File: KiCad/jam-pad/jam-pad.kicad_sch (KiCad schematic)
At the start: 61 parts

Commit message: update gitignore, some unknown schematic changes
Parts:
- added J?: Conn_01x03, symbol Connector_Generic:Conn_01x03
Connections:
- net DIG0 is gone; now on net Row0: U?.2 (GPIO0)
- net DIG1 is gone; now on net Row1: U?.3 (GPIO1)
- net DIG10 is gone; now on net CS: U?.13 (GPIO10)
- net DIG11 is gone; now on net DC: U?.14 (GPIO11)
- net DIG12 is gone; now on net OLED_RST: U?.15 (GPIO12)
- net DIG13 is gone; now on net ENC_A: U?.16 (GPIO13)
- net DIG14 is gone; now on net ENC_C: U?.17 (GPIO14)
- net DIG15 is gone; now on net ENC_B: U?.18 (GPIO15)
- net DIG2 is gone; now on net Row2: U?.4 (GPIO2)
- net DIG3 is gone; now on net Col0: U?.5 (GPIO3)
- net DIG4 is gone; now on net Col1: U?.6 (GPIO4)
- net DIG5 is gone; now on net Col2: U?.7 (GPIO5)
- net DIG6 is gone; now on net Col3: U?.8 (GPIO6)
- net DIG7 is gone; now on net Col4: U?.9 (GPIO7)
- net DIG8 is gone; now on net MOSI: U?.11 (GPIO8)
- net DIG9 is gone; now on net SCLK: U?.12 (GPIO9)
- net GND: now also J?.2 (Pin_2)
- net SWCLK: now also J?.3 (Pin_3)
- net SWDIO: now also J?.1 (Pin_1)
- net at U?.21 (XOUT): now also C?.2, Y?.1
- net ~{DIR_OUT_A}: no longer names the net of U?.27 (GPIO16)
- net ~{DIR_OUT_B}: no longer names the net of U?.29 (GPIO18)
- net ~{OE_A}: no longer names the net of U?.28 (GPIO17)
- net ~{OE_B}: no longer names the net of U?.30 (GPIO19)
- no-connect marks 5 -> 9

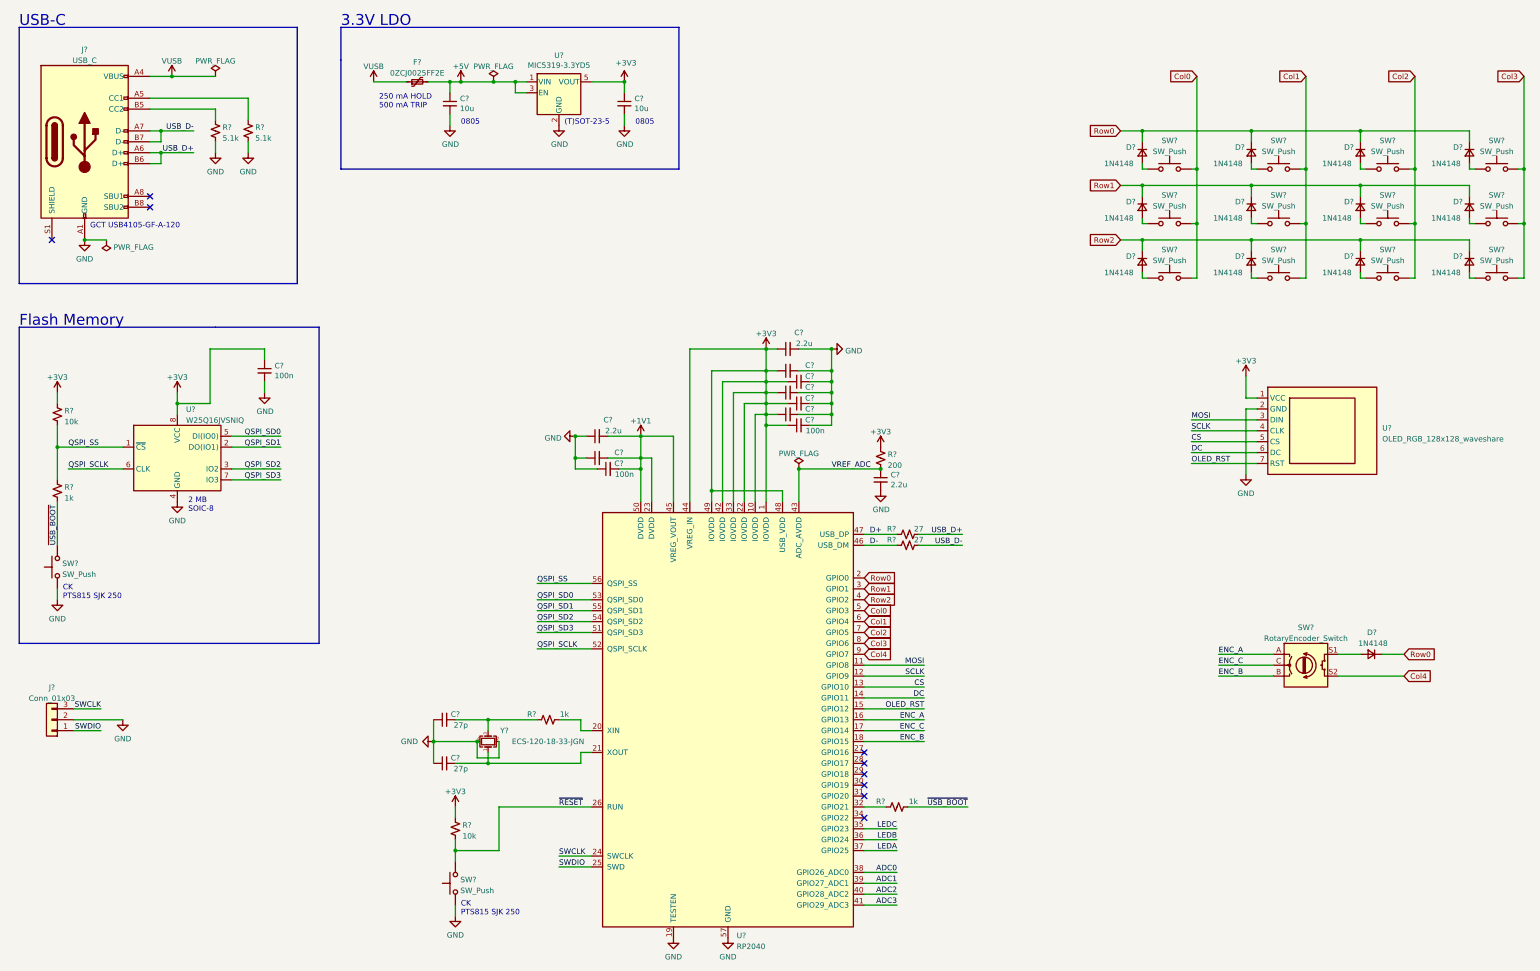
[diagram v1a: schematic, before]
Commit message: Assign footprints
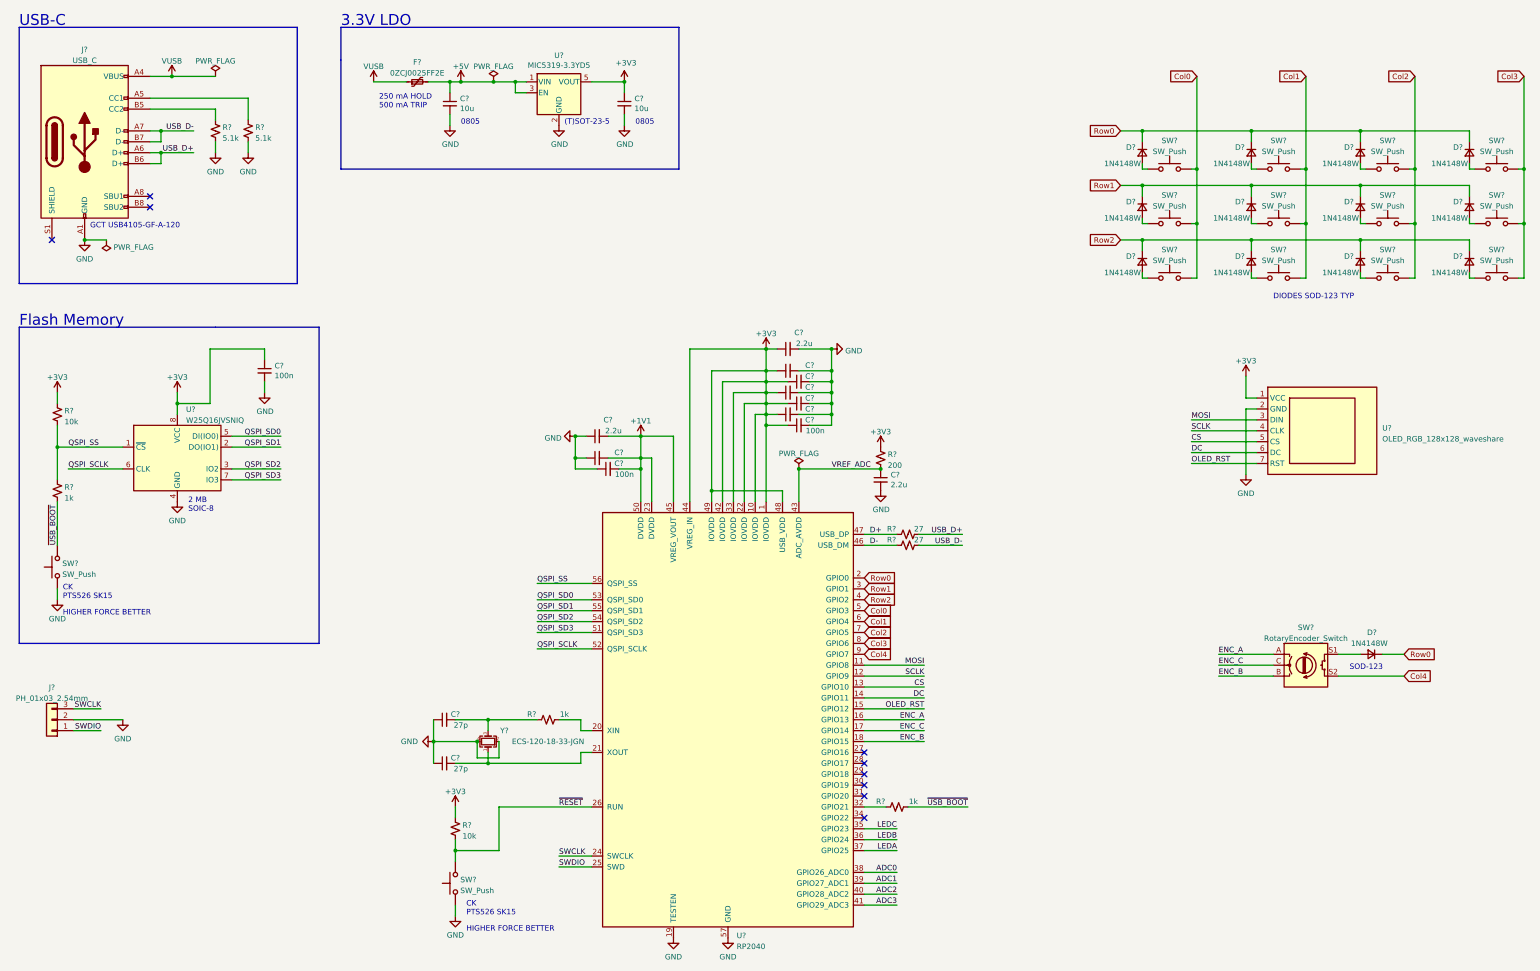
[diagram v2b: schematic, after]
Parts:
- D? (x13): value 1N4148 -> 1N4148W; footprint (none) -> Diode_SMD:D_SOD-123
- J?: value Conn_01x03 -> PH_01x03_2.54mm; footprint (none) -> jam-pad:PinHeader_1x03_P2.54mm_NoSilk
- SW? (x12): footprint (none) -> Keebio-Parts:Kailh-PG1350-1u-NoLED
- SW? (x2): footprint jackrabbit:SW_Push_CK_PTS815_HandSoldering -> jam-pad:SW_Push_PTS526
- SW?: footprint (none) -> Rotary_Encoder:RotaryEncoder_Alps_EC11E-Switch_Vertical_H20mm
- U?: footprint (none) -> jam-pad:Display_Waveshare_OLED_1.5inch_128x128
- U?: footprint jackrabbit:RP2040-QFN-56_HandSoldering -> jam-pad:RP2040-QFN-56_HandSoldering
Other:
- note added: "CK PTS526 SK15"
- note added: "DIODES SOD-123 TYP"
- note added: "HIGHER FORCE BETTER"
- note added: "SOD-123"
- note removed: "CK PTS815 SJK 250"
- title: (none) -> JamPad

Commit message: mx_only fp lib and replace switch footprints
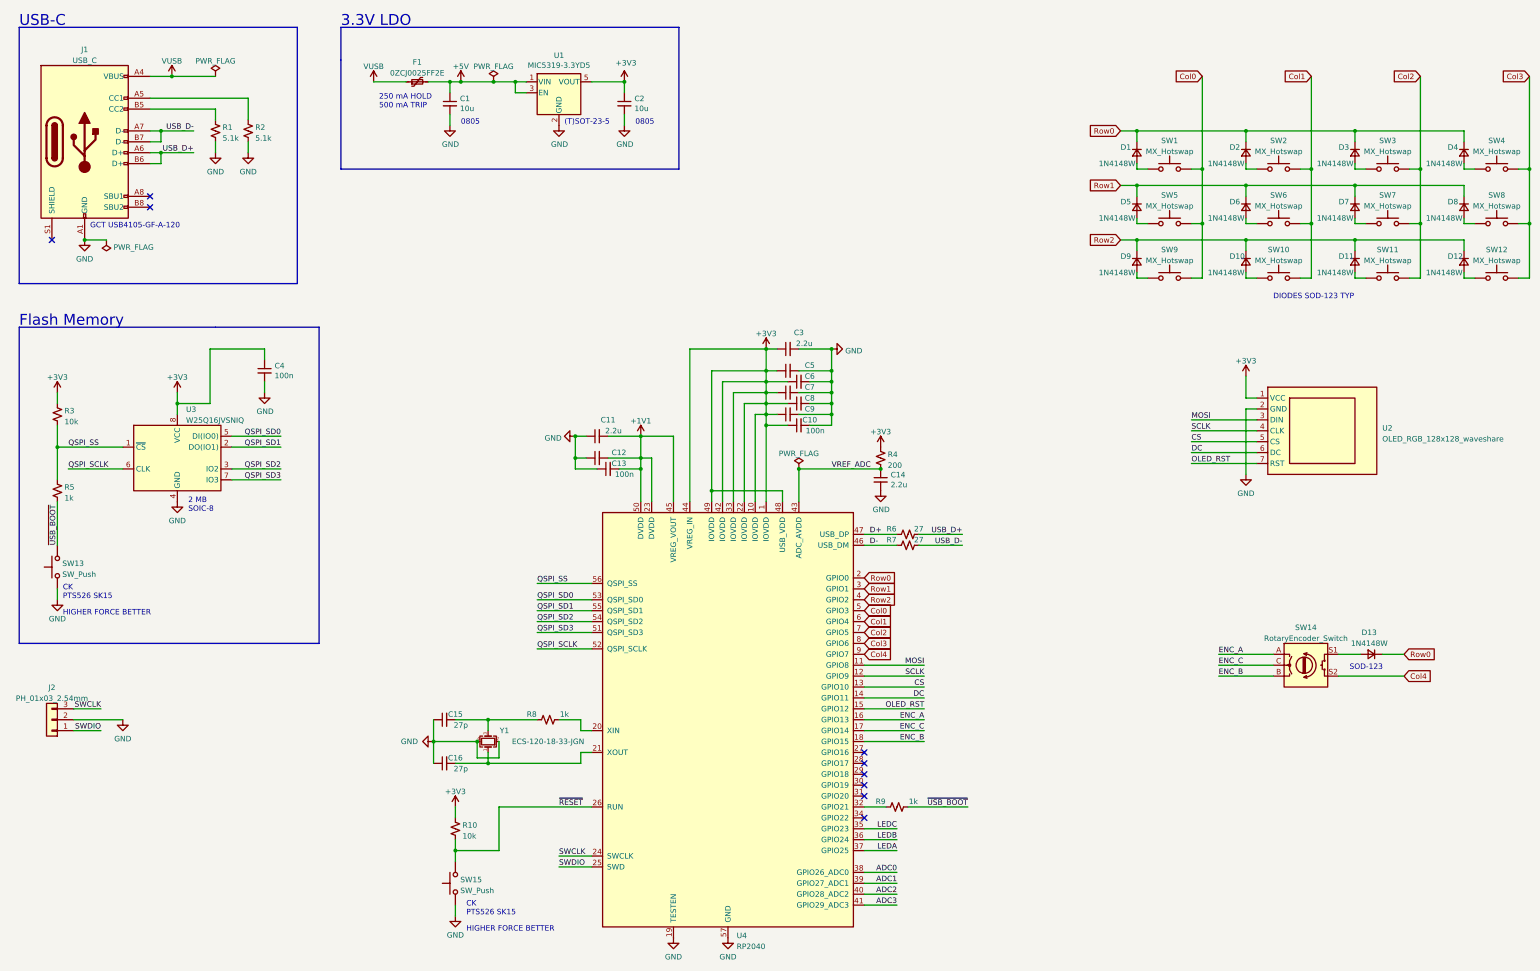
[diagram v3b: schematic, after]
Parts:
- SW1, SW10, SW11, SW12, SW2, SW3, SW4, SW5, SW6, SW7, SW8, SW9: renamed from SW?; value SW_Push -> MX_Hotswap; footprint Keebio-Parts:Kailh-PG1350-1u-NoLED -> MX_Only:MXOnly-1U-Hotswap-LED
- gave numbers to parts that had none: 50
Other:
- moved on the sheet: D1, D10, D11, D12, D2, D3, D4, D5, D6, D7, D8, D9

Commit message: Clean up symbol dependencies and pass ERC with schematic so far
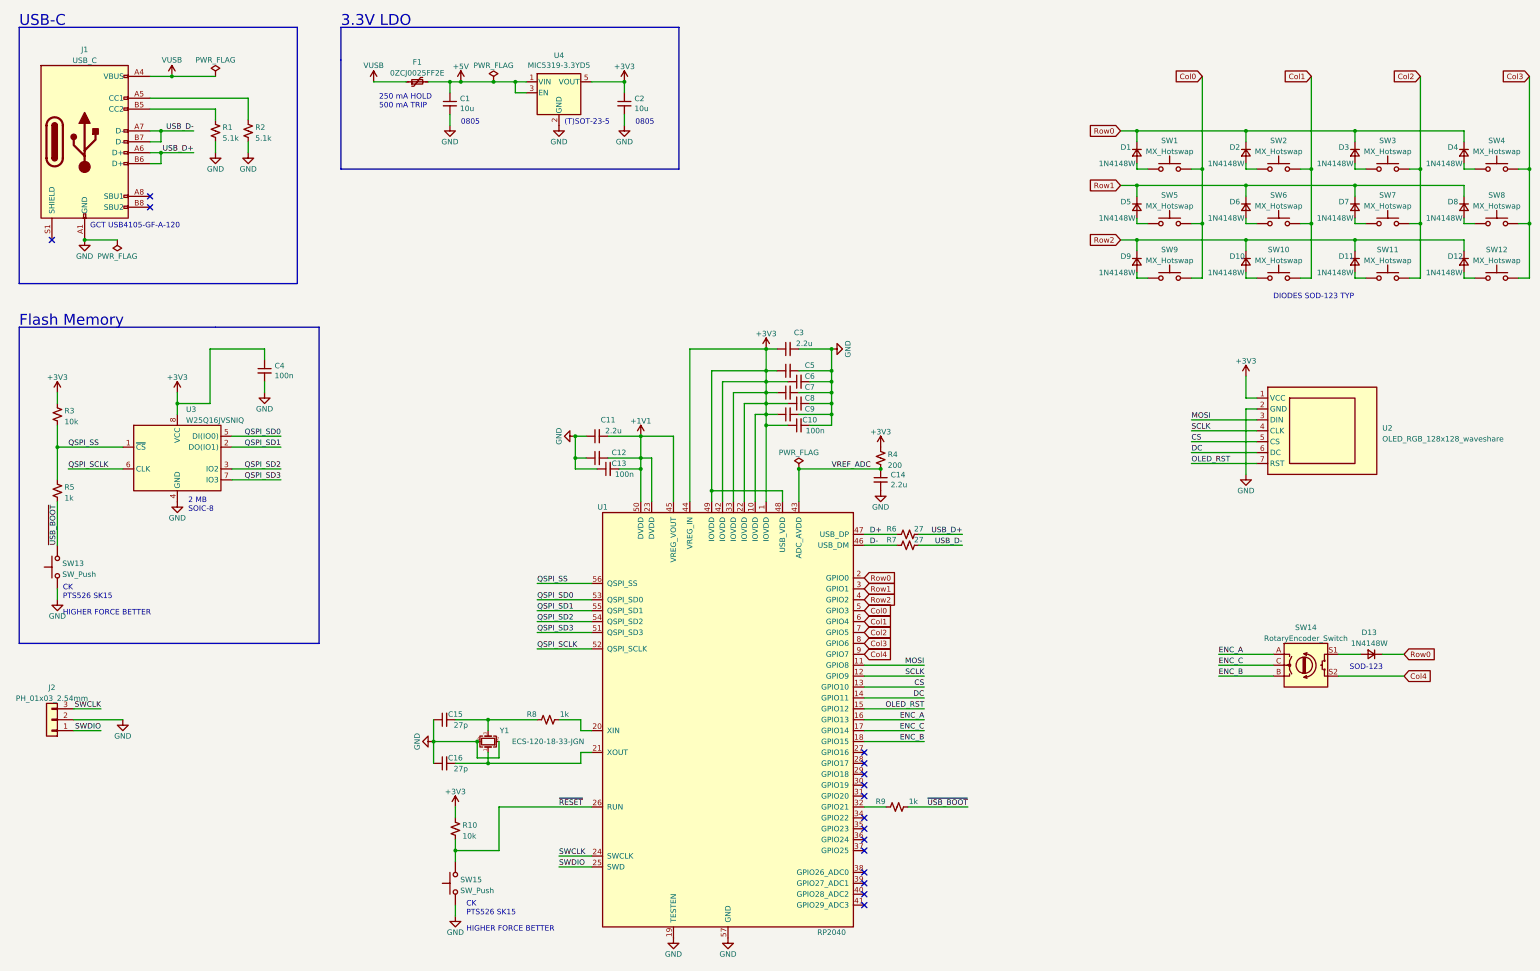
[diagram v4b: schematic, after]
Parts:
- J1: footprint jackrabbit:USB_C_Receptacle_GCT_USB4105-GF-A-120 -> jam-pad:USB_C_Receptacle_GCT_USB4105-GF-A-120
- U1: renamed from U4; footprint jam-pad:RP2040-QFN-56_HandSoldering -> jackrabbit:RP2040-QFN-56_HandSoldering; symbol jackrabbit:RP2040 -> jam-pad:RP2040
- renumbered U1 to U4
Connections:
- net ADC0: no longer names the net of U1.38 (GPIO26_ADC0)
- net ADC1: no longer names the net of U1.39 (GPIO27_ADC1)
- net ADC2: no longer names the net of U1.40 (GPIO28_ADC2)
- net ADC3: no longer names the net of U1.41 (GPIO29_ADC3)
- net LEDA: no longer names the net of U1.37 (GPIO25)
- net LEDB: no longer names the net of U1.36 (GPIO24)
- net LEDC: no longer names the net of U1.35 (GPIO23)
- no-connect marks 9 -> 16
